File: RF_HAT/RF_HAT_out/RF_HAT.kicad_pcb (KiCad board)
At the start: 2 copper layers, 55 x 65 mm, 89 parts, among them J1 SMA, J2 SMA, J3 Raspberry_Pi_2_3, U1 CC1200RHBR, U2 CC1200RHBR, U3 RaspberryPi_Pico, Y1 40MHz, Y2 40MHz

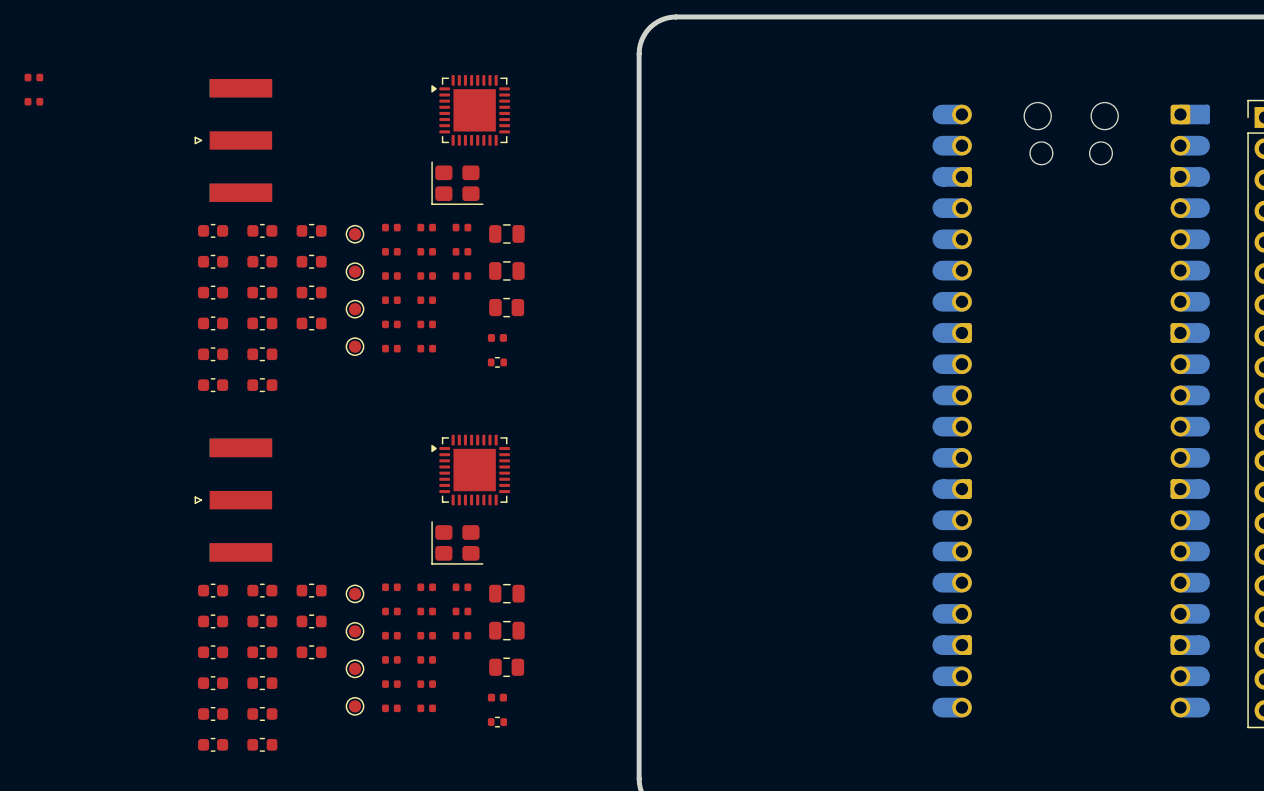
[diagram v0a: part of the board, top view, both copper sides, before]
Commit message: switch to SMD pico
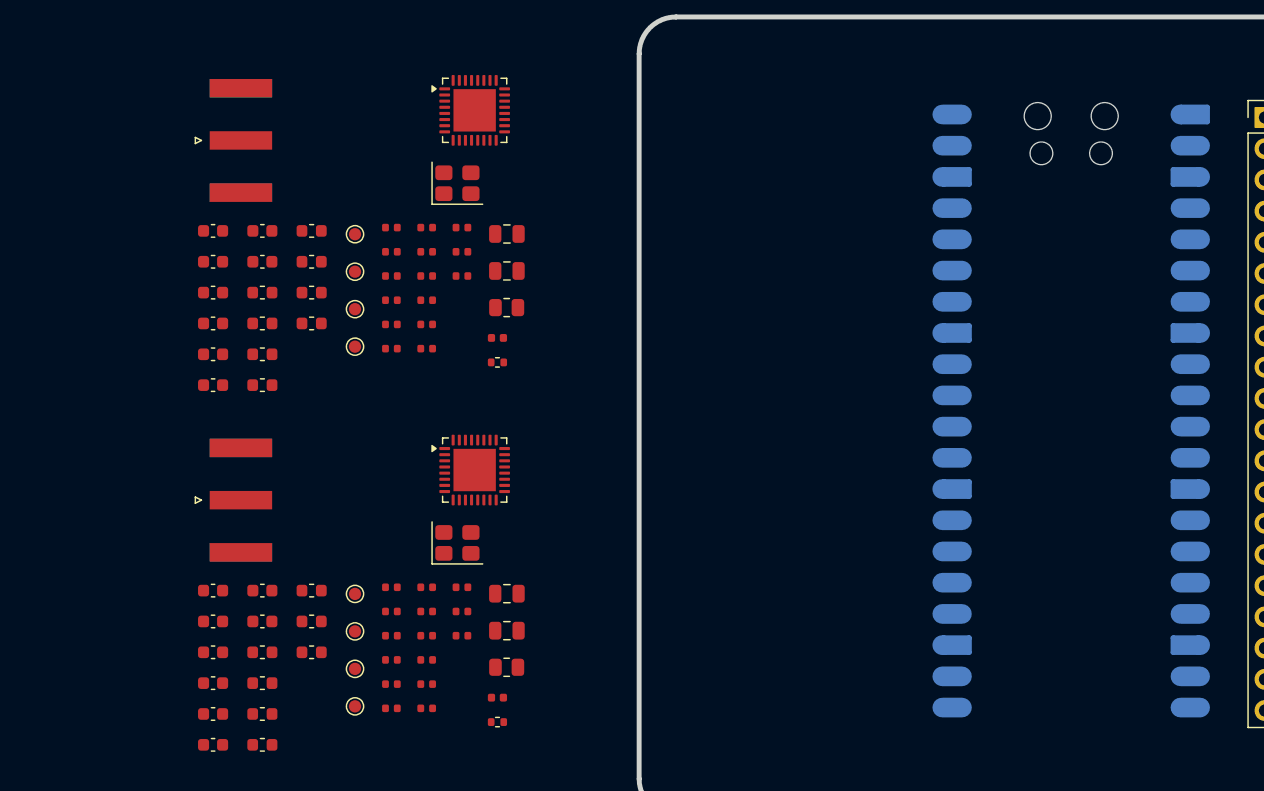
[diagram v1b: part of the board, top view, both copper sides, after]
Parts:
- removed C51, C52: 100nF, Capacitor_SMD:C_0402_1005Metric
- U3: footprint Module:RaspberryPi_Pico_Common_Unspecified -> Module:RaspberryPi_Pico_Common_SMD

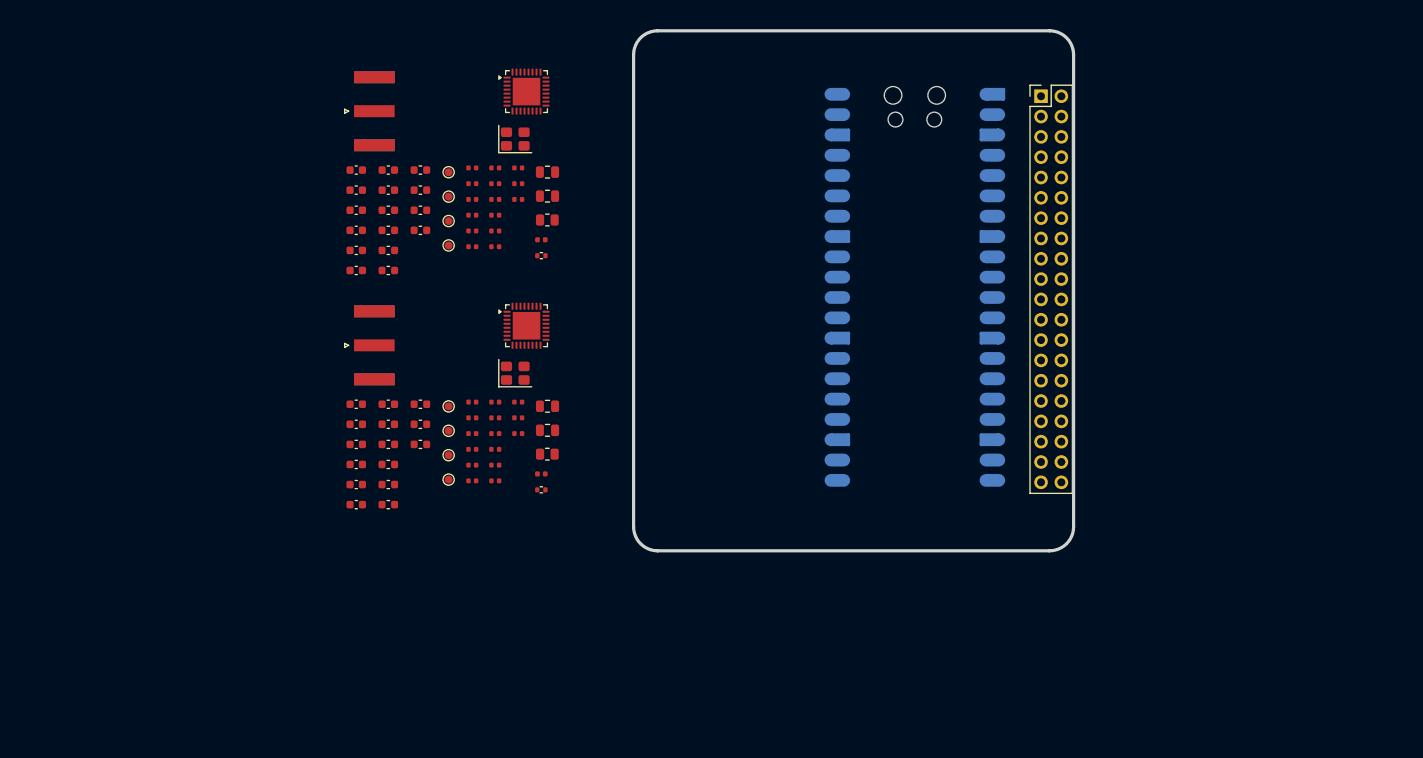
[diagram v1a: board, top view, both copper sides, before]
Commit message: switched to 0603 for all passives
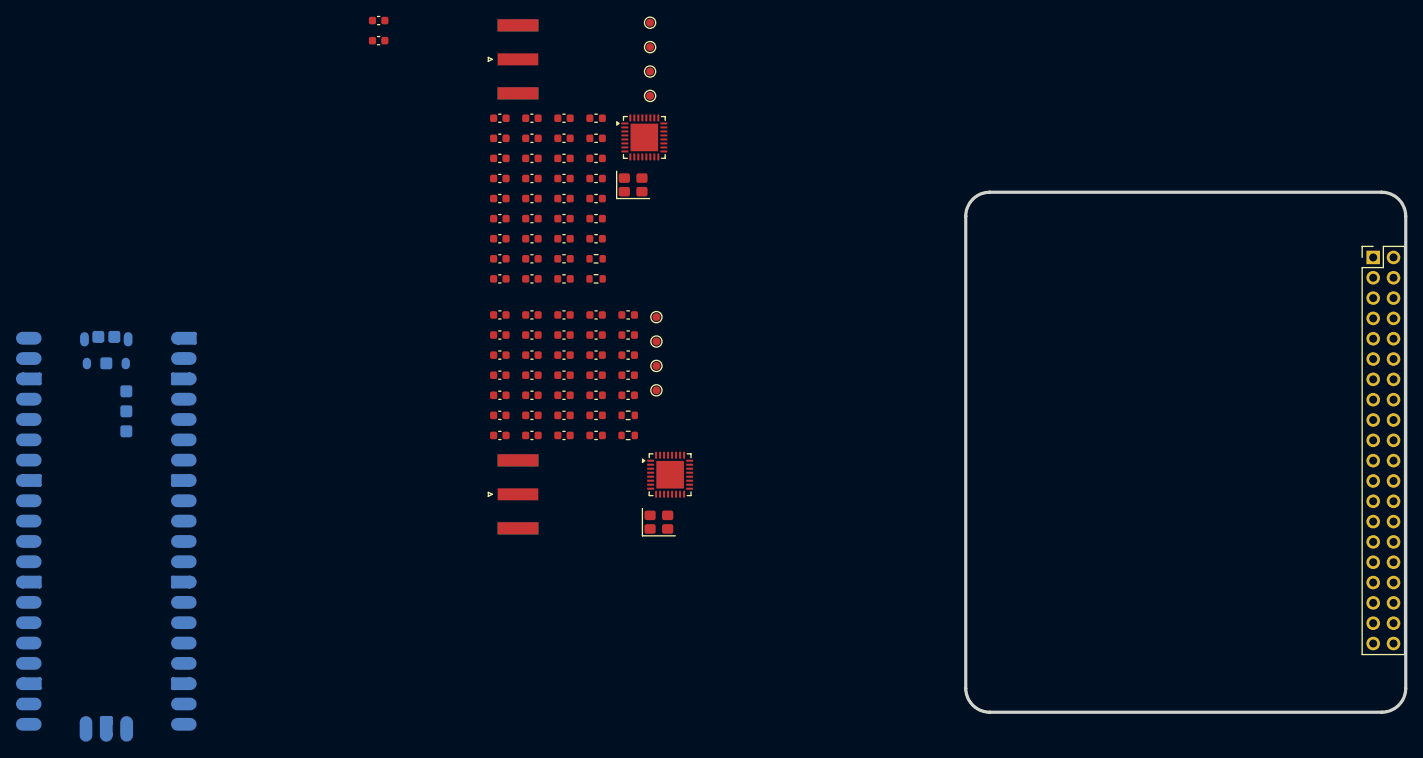
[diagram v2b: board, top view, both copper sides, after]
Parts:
- added C51: 100nF, Capacitor_SMD:C_0603_1608Metric, F.Cu at (89.3, 39.4)
- added C52: 100nF, Capacitor_SMD:C_0603_1608Metric, F.Cu at (89.3, 41.9)
- C1, C2, C26, C27: footprint Capacitor_SMD:C_0805_2012Metric -> Capacitor_SMD:C_0603_1608Metric
- C10, C11, C12, C13, C14, C15, C16, C17, C28, C29, C3, C30, C31, C32, C33, C34, C35, C36, C37, C38, C39, C4, C40, C41, C42, C5, C6, C7, C8, C9: footprint Capacitor_SMD:C_0402_1005Metric -> Capacitor_SMD:C_0603_1608Metric
- C44: value 18pF -> 100pF
- FB1, FB2: footprint Inductor_SMD:L_0402_1005Metric -> Inductor_SMD:L_0603_1608Metric
- L15: value 100nH -> 47nH
- R1, R3: footprint Resistor_SMD:R_0402_1005Metric -> Resistor_SMD:R_0603_1608Metric
- R2, R4: footprint Resistor_SMD:R_0805_2012Metric -> Resistor_SMD:R_0603_1608Metric
- U3: footprint Module:RaspberryPi_Pico_Common_SMD -> Module:RaspberryPi_Pico_SMD
- moved U3 105.6 mm to (55.3, 103.2)
- moved J3 46.2 mm to (213.6, 69.0)
- moved C47 36.7 mm to (116.5, 76.2)
- moved C48 36.7 mm to (116.5, 78.7)
- moved L11 36.7 mm to (120.5, 76.2)
- moved L12 36.7 mm to (120.5, 78.7)
- moved TP4 31.4 mm to (123.2, 48.8)
- moved TP1 31.4 mm to (123.2, 39.7)
- moved TP2 31.4 mm to (123.2, 42.7)
- moved TP3 31.4 mm to (123.2, 45.8)
- moved L2 29.5 mm to (116.5, 51.6)
- moved L3 29.5 mm to (116.5, 54.1)
- moved L4 29.5 mm to (116.5, 56.6)
- moved TP6 28.3 mm to (124.0, 79.5)
- moved TP7 28.3 mm to (124.0, 82.6)
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
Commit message: first routing of signals
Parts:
- removed C51, C52: 100nF, Capacitor_SMD:C_0603_1608Metric
- removed TP1, TP2, TP3, TP4, TP5, TP6, TP7, TP8: ~, TestPoint:TestPoint_Pad_D1.0mm
- added H1: MountingHole_Pad, MountingHole:MountingHole_2.7mm_M2.5_ISO14580_Pad, F.Cu at (165.7, 64.3)
- added H2: MountingHole_Pad, MountingHole:MountingHole_2.7mm_M2.5_ISO14580_Pad, F.Cu at (214.7, 64.3)
- added H3: MountingHole_Pad, MountingHole:MountingHole_2.7mm_M2.5_ISO14580_Pad, F.Cu at (165.7, 122.3)
- added H4: MountingHole_Pad, MountingHole:MountingHole_2.7mm_M2.5_ISO14580_Pad, F.Cu at (214.7, 122.3)
- moved U3 145.5 mm to (199.9, 88.0)
- moved J1 121.4 mm to (198.7, 123.5), turned to -90 degrees
- moved C1 116.3 mm to (208.8, 103.0), turned to 90 degrees
- moved C10 114.5 mm to (208.0, 108.2)
- moved C5 114.1 mm to (208.0, 109.6)
- moved C19 112.2 mm to (204.1, 116.3), turned to -90 degrees
- moved C20 112.0 mm to (208.0, 112.6)
- moved C21 112.0 mm to (207.2, 116.3), turned to 90 degrees
- moved C2 111.6 mm to (206.5, 99.3)
- moved C6 111.4 mm to (208.0, 105.2)
- moved C4 110.1 mm to (201.4, 111.3), turned to -90 degrees
- moved L4 109.9 mm to (208.7, 116.3), turned to -90 degrees
- moved C7 109.7 mm to (204.7, 111.3), turned to 90 degrees
- moved C9 109.3 mm to (208.0, 106.7)
- moved C22 109.2 mm to (205.6, 116.3), turned to 90 degrees
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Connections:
- C10 pad 1: /+3.3V -> /CC1200_UHF_432MHz/UHF_AVDD_FILT
- C11 pad 1: /+3.3V -> /CC1200_UHF_432MHz/UHF_AVDD_FILT
- C12 pad 1: /+3.3V -> /CC1200_UHF_432MHz/UHF_AVDD_FILT
- C13 pad 1: /+3.3V -> /CC1200_UHF_432MHz/UHF_AVDD_FILT
- C14 pad 1: /+3.3V -> /CC1200_UHF_432MHz/UHF_AVDD_FILT
- C15 pad 1: /+3.3V -> /CC1200_UHF_432MHz/UHF_AVDD_FILT
- C16 pad 1: /+3.3V -> /CC1200_UHF_432MHz/UHF_AVDD_FILT
- C33 pad 1: /+3.3V -> /CC1200_VHF_144MHz/VHF_AVDD_FILT
- C34 pad 1: /+3.3V -> /CC1200_VHF_144MHz/VHF_AVDD_FILT
- C35 pad 1: /+3.3V -> /CC1200_VHF_144MHz/VHF_AVDD_FILT
- C36 pad 1: /+3.3V -> /CC1200_VHF_144MHz/VHF_AVDD_FILT
- C37 pad 1: /+3.3V -> /CC1200_VHF_144MHz/VHF_AVDD_FILT
- C38 pad 1: /+3.3V -> /CC1200_VHF_144MHz/VHF_AVDD_FILT
- C39 pad 1: /+3.3V -> /CC1200_VHF_144MHz/VHF_AVDD_FILT
- C40 pad 1: /+3.3V -> /CC1200_VHF_144MHz/VHF_AVDD_FILT
- C41 pad 1: /+3.3V -> /CC1200_VHF_144MHz/VHF_AVDD_FILT
- C8 pad 1: /+3.3V -> /CC1200_UHF_432MHz/UHF_AVDD_FILT
- C9 pad 1: /+3.3V -> /CC1200_UHF_432MHz/UHF_AVDD_FILT
- U1 pad 1: /+3.3V -> /CC1200_UHF_432MHz/UHF_AVDD_FILT
- U1 pad 12: unconnected-(U1-DVDD-Pad12) -> /CC1200_UHF_432MHz/UHF_AVDD_FILT
- U1 pad 13: /+3.3V -> /CC1200_UHF_432MHz/UHF_AVDD_FILT
- U1 pad 15: /+3.3V -> /CC1200_UHF_432MHz/UHF_AVDD_FILT
- U1 pad 22: /+3.3V -> /CC1200_UHF_432MHz/UHF_AVDD_FILT
- U1 pad 25: /+3.3V -> /CC1200_UHF_432MHz/UHF_AVDD_FILT
- U1 pad 27: /+3.3V -> /CC1200_UHF_432MHz/UHF_AVDD_FILT
- U1 pad 28: /+3.3V -> /CC1200_UHF_432MHz/UHF_AVDD_FILT
- U1 pad 5: /+3.3V -> /CC1200_UHF_432MHz/UHF_AVDD_FILT
- U2 pad 1: /+3.3V -> /CC1200_VHF_144MHz/VHF_AVDD_FILT
- U2 pad 12: unconnected-(U2-DVDD-Pad12) -> /CC1200_VHF_144MHz/VHF_AVDD_FILT
- U2 pad 13: /+3.3V -> /CC1200_VHF_144MHz/VHF_AVDD_FILT
- U2 pad 15: /+3.3V -> /CC1200_VHF_144MHz/VHF_AVDD_FILT
- U2 pad 22: /+3.3V -> /CC1200_VHF_144MHz/VHF_AVDD_FILT
- U2 pad 25: /+3.3V -> /CC1200_VHF_144MHz/VHF_AVDD_FILT
- U2 pad 27: /+3.3V -> /CC1200_VHF_144MHz/VHF_AVDD_FILT
- U2 pad 28: /+3.3V -> /CC1200_VHF_144MHz/VHF_AVDD_FILT
- U2 pad 5: /+3.3V -> /CC1200_VHF_144MHz/VHF_AVDD_FILT
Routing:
- net /+3.3V: track 0.00 -> 62.9 mm, vias 0 -> 1
- net /GND: track 0.00 -> 59.5 mm, vias 0 -> 169
- net /CC1200_UHF_432MHz/UHF_AVDD_FILT: track 0.00 -> 35.9 mm, vias 0 -> 9
- net /CC1200_VHF_144MHz/VHF_AVDD_FILT: track 0.00 -> 34.3 mm, vias 0 -> 11
- net /UHF_GPIO3: track 0.00 -> 24.3 mm, vias 0 -> 1
- net /UHF_GPIO0: track 0.00 -> 22.8 mm, vias 0 -> 2
- net /VHF_GPIO3: track 0.00 -> 22.3 mm, vias 0 -> 2
- net /VHF_GPIO0: track 0.00 -> 20.4 mm, vias 0 -> 2
- net /CC1200_UHF_432MHz/UHF_LN7: track 0.00 -> 18.7 mm
- net /UHF_GPIO2: track 0.00 -> 18.0 mm, vias 0 -> 1
- net /CC1200_VHF_144MHz/VHF_LN6: track 0.00 -> 17.8 mm
- net /UHF_RESET: track 0.00 -> 17.6 mm, vias 0 -> 1
- net /VHF_MISO: track 0.00 -> 14.8 mm, vias 0 -> 1
- net /UHF_SCLK: track 0.00 -> 14.4 mm, vias 0 -> 1
- net /UHF_CSN: track 0.00 -> 14.0 mm, vias 0 -> 2
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- added copper zone on In4.Cu, net /CC1200_UHF_432MHz/UHF_AVDD_FILT
- added copper zone on In4.Cu, net /CC1200_VHF_144MHz/VHF_AVDD_FILT
- added copper zone on In1.Cu, net /GND
- added copper zone on In3.Cu, net /GND
- added copper zone on In5.Cu, net /GND
- added copper zone on In6.Cu, net /GND
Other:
- board size 55 x 65 mm -> 56 x 65 mm
- copper layers 2 -> 8
- board text added: "UHF"
- board text added: "VHF"
